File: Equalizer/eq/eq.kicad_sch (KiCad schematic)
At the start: 48 parts, among them J1 Conn_01x04_Pin, U1 TL074, U2 TL074

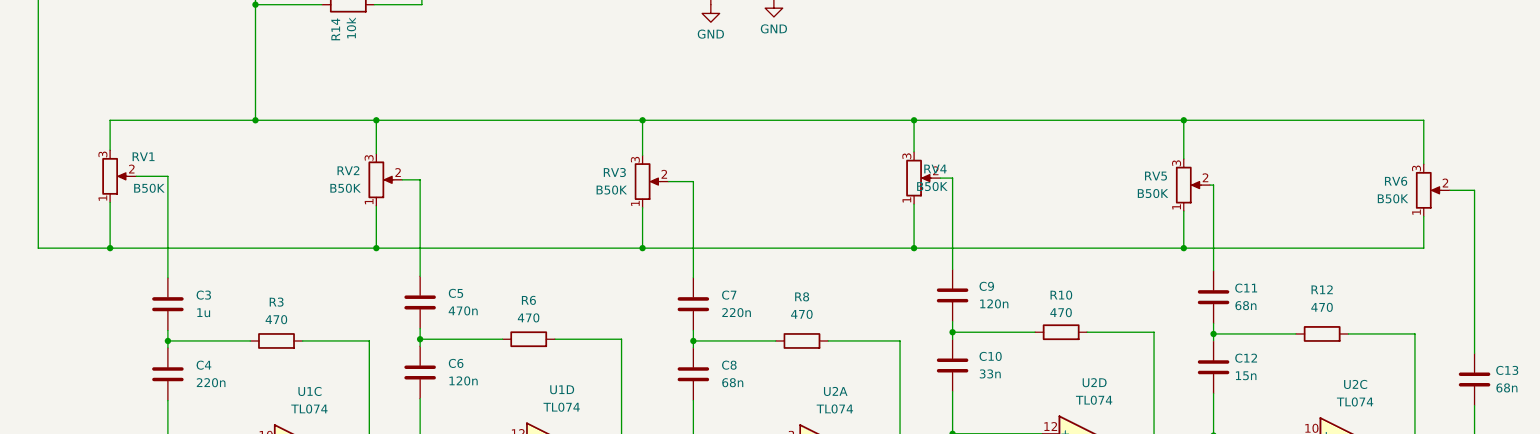
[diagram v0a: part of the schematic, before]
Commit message: added engineers thumb, ramshead-bmp
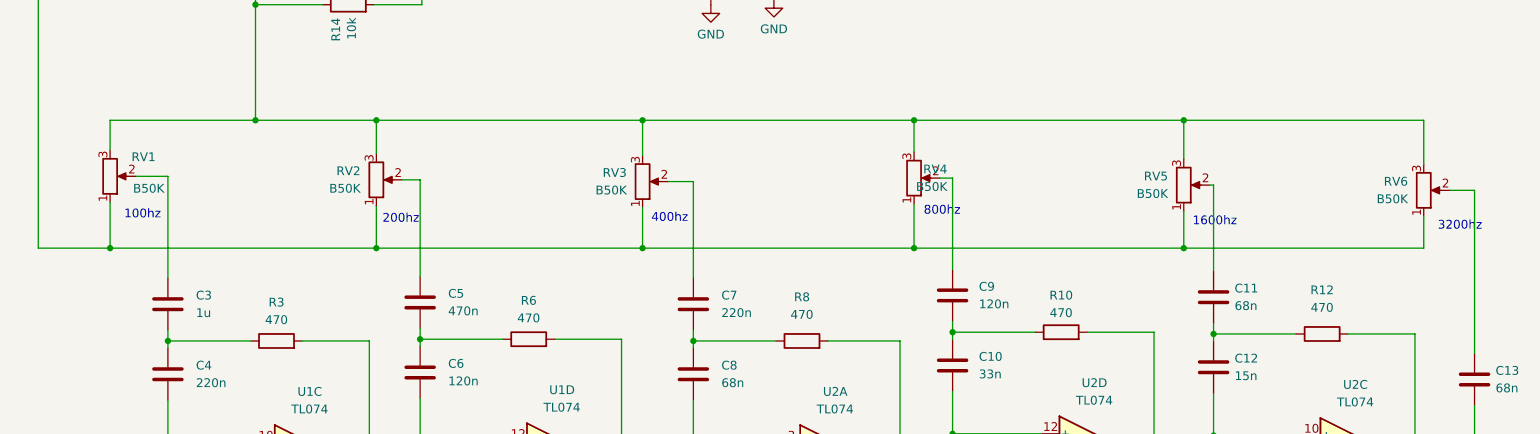
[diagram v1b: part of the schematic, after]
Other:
- note added: "100hz"
- note added: "1600hz"
- note added: "200hz"
- note added: "3200hz"
- note added: "400hz"
- note added: "800hz"
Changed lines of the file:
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@@
     (stroke (width 0) (type default))
+  )
+  (text "800hz\n\n\n" (at 195.707 95.758 0)
+    (effects (font (size 1.27 1.27)) (justify left bottom))
+  )
+  (text "1600hz\n\n" (at 234.696 95.25 0)
+    (effects (font (size 1.27 1.27)) (justify left bottom))
+  )
+  (text "3200hz\n\n" (at 270.256 95.885 0)
+    (effects (font (size 1.27 1.27)) (justify left bottom))
+  )
+  (text "100hz" (at 79.756 92.202 0)
+    (effects (font (size 1.27 1.27)) (justify left bottom))
+  )
+  (text "400hz\n" (at 156.21 92.71 0)
+    (effects (font (size 1.27 1.27)) (justify left bottom))
+  )
+  (text "200hz\n" (at 117.221 92.837 0)
+    (effects (font (size 1.27 1.27)) (justify left bottom))
   )
   (global_label "VB" (shape input) (at 199.898 132.588 270) (fields_autoplaced)
